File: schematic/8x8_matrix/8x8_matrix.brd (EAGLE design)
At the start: 160 x 101.3 mm, 69 parts, among them U1 ATTINY85-20PU

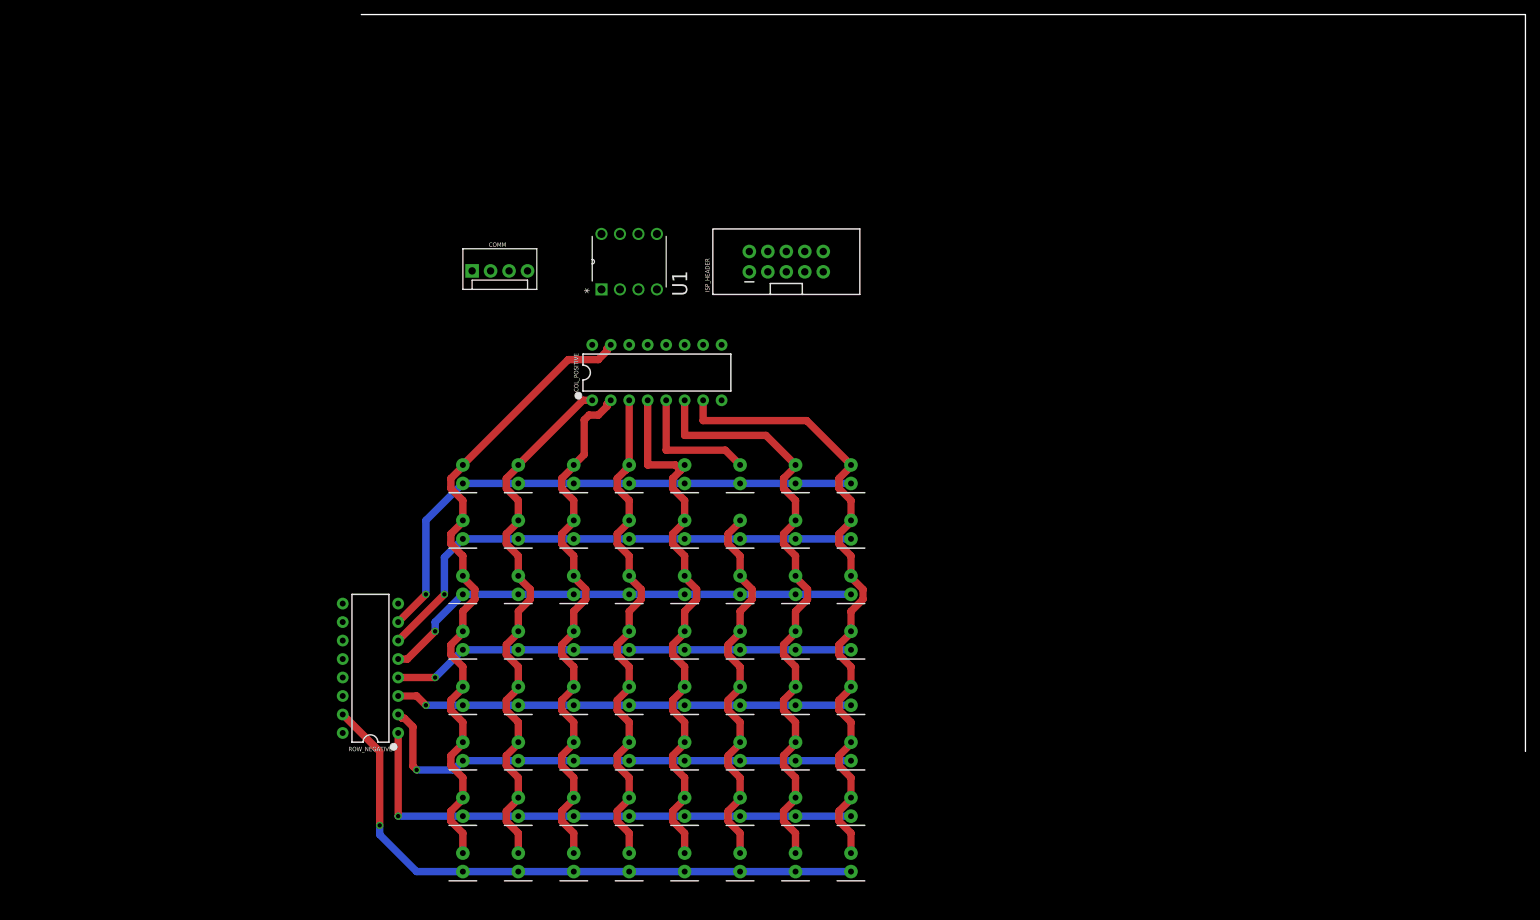
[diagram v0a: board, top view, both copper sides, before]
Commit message: _Serial now reads and writes bytes instead of data_packet
The work of assembling data_packet is now in the main loop instead of in _Serial
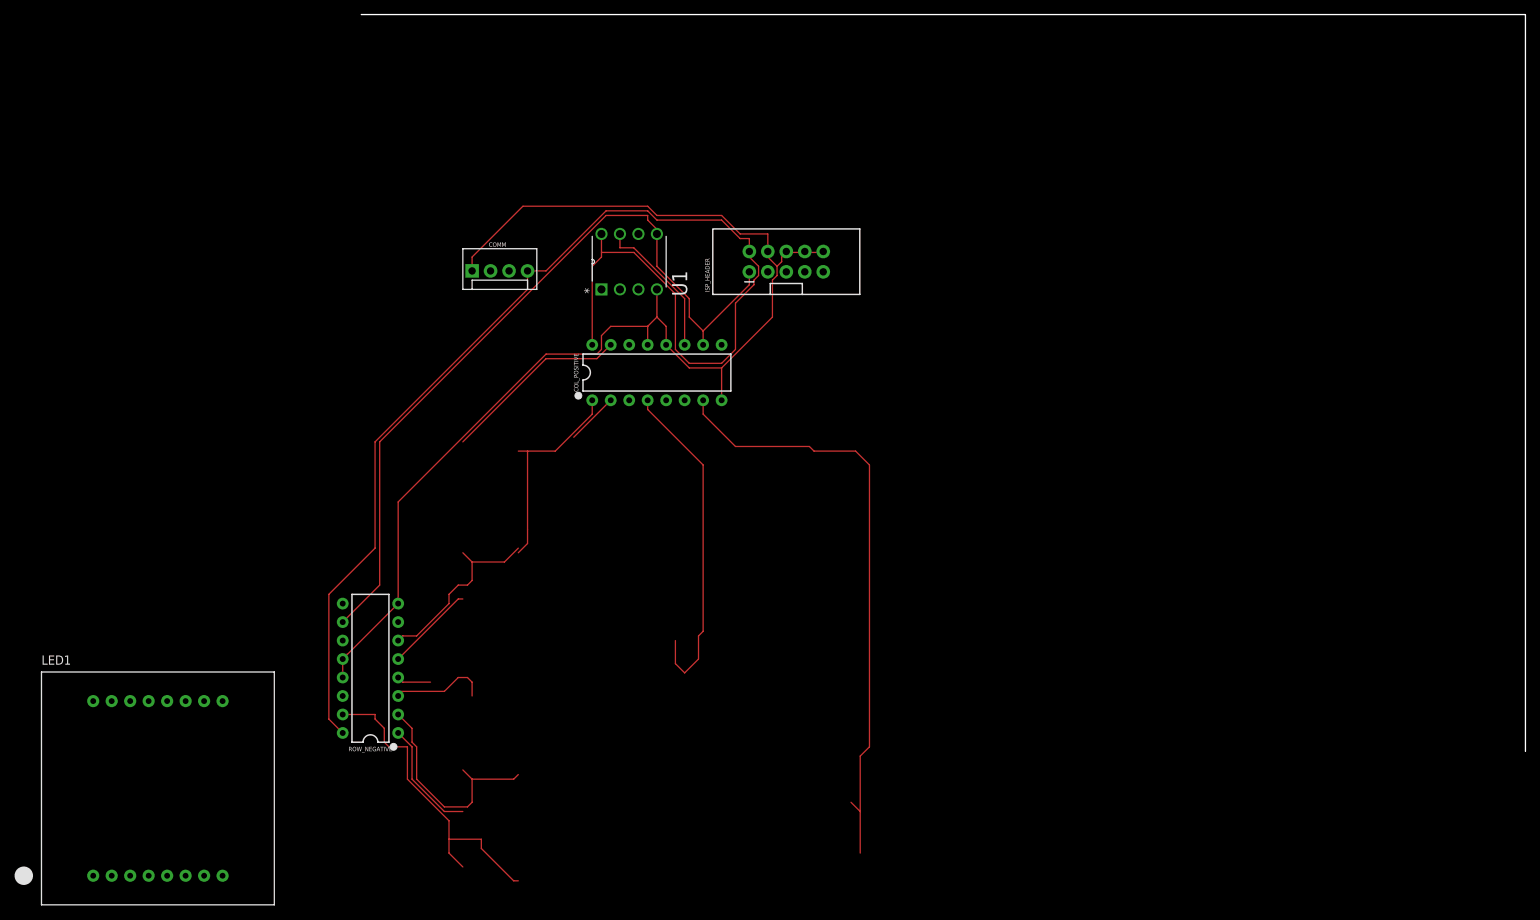
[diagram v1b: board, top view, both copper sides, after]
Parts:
- removed D1, D10, D11, D12, D13, D14, D15, D16, D17, D18, D19, D2, D20, D21, D22, D23, D24, D25, D26, D27, D28, D29, D3, D30, D31, D32, D33, D34, D35, D36, D37, D38, D39, D4, D40, D41, D42, D43, D44, D45, D46, D47, D48, D49, D5, D50, D51, D52, D53, D54, D55, D56, D57, D58, D59, D6, D60, D61, D62, D63, D64, D7, D8, D9: (no value), SparkFun-LED:LED_5MM-KIT
- added LED1: (no value), adafruit:SEGMENT_BL-M12A881UR
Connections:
- net COL1: no longer D1.A, D17.A, D25.A, D33.A, D41.A, D49.A, D57.A, D9.A
- net COL2: no longer D10.A, D18.A, D2.A, D26.A, D34.A, D42.A, D50.A, D58.A
- net COL3: no longer D11.A, D19.A, D27.A, D3.A, D35.A, D43.A, D51.A, D59.A
- net COL4: no longer D12.A, D20.A, D28.A, D36.A, D4.A, D44.A, D52.A, D60.A
- net COL5: no longer D13.A, D21.A, D29.A, D37.A, D45.A, D5.A, D53.A, D61.A
- net COL6: no longer D14.A, D22.A, D30.A, D38.A, D46.A, D54.A, D6.A, D62.A
- net COL7: no longer D15.A, D23.A, D31.A, D39.A, D47.A, D55.A, D63.A, D7.A
- net COL8: no longer D16.A, D24.A, D32.A, D40.A, D48.A, D56.A, D64.A, D8.A
- net ROW1: no longer D1.K, D2.K, D3.K, D4.K, D5.K, D6.K, D7.K, D8.K
- net ROW2: no longer D10.K, D11.K, D12.K, D13.K, D14.K, D15.K, D16.K, D9.K
- net ROW3: no longer D17.K, D18.K, D19.K, D20.K, D21.K, D22.K, D23.K, D24.K
- net ROW4: no longer D25.K, D26.K, D27.K, D28.K, D29.K, D30.K, D31.K, D32.K
- net ROW5: no longer D33.K, D34.K, D35.K, D36.K, D37.K, D38.K, D39.K, D40.K
- net ROW6: no longer D41.K, D42.K, D43.K, D44.K, D45.K, D46.K, D47.K, D48.K
- net ROW7: no longer D49.K, D50.K, D51.K, D52.K, D53.K, D54.K, D55.K, D56.K
- net ROW8: no longer D57.K, D58.K, D59.K, D60.K, D61.K, D62.K, D63.K, D64.K
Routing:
- net GND: track 0.00 -> 175.9 mm
- net VCC: track 0.00 -> 173.9 mm
- net ISP_MOSI/SCL: track 0.00 -> 108.3 mm
- net COL7: track 84.7 -> 0.00 mm
- net ROW8: track 76.1 -> 0.00 mm, vias 1 -> 0
- net COL4: track 72.8 -> 0.00 mm
- net COL6: track 71.8 -> 0.00 mm
- net COL3: track 74.9 -> 7.18 mm
- net COL1: track 90.3 -> 25.8 mm
- net ROW5: track 63.8 -> 4.71 mm, vias 1 -> 0
- net ROW2: track 73.7 -> 16.0 mm, vias 1 -> 0
- net ROW6: track 66.7 -> 12.3 mm, vias 1 -> 0
- net ROW4: track 62.8 -> 13.8 mm, vias 1 -> 0
- net COL2: track 76.8 -> 28.7 mm
- net ROW7: track 71.0 -> 25.8 mm, vias 1 -> 0
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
